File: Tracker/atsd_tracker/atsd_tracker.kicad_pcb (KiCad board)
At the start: 2 copper layers, 54 parts, among them J101 ICSP, J102 Battery, J103 SMA_PCB, Q101 IRLML2244, U101 MCP73821_2_SOT-23-5, U102 AZ1117CR-X.XTRG1, U103 DSPIC33CK64MC105, U104 AX5243, X101 16MHz, X102 8MHz

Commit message: Schematic done starting layout
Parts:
- added C121: 10pF, General_SMD:SM0402, F.Cu at (69.2, 87.8)
- added C122: 10pF, General_SMD:SM0402, F.Cu at (69.2, 90.5)
- added D103: RED, General_SMD:LED-0603, F.Cu at (92.2, 82.0)
- added D104: BLUE, General_SMD:LED-0603, F.Cu at (90.6, 82.0)
- added D105: GREEN, General_SMD:LED-0603, F.Cu at (89.0, 82.0)
- added J101: 5V Connector, Connector_JST:JST_XH_B2B-XH-A_1x02_P2.50mm_Vertical, F.Cu at (68.7, 109.4)
- added J103: Left side, Connector_PinHeader_1.27mm:PinHeader_2x05_P1.27mm_Vertical, F.Cu at (95.2, 83.6)
- added J104: Right side, Connector_PinHeader_1.27mm:PinHeader_2x05_P1.27mm_Vertical, F.Cu at (95.2, 105.6)
- added J106: SMA_PCB, Connectors_RF:SMA_RA_PCB_Amphenol, F.Cu at (61.6, 87.8)
- added L103: NC, General_SMD:SM0402, F.Cu at (120.6, 94.7)
- added L107: IND_0402, General_SMD:SM0402, F.Cu at (68.0, 88.2)
- added R103: 100, General_SMD:SM0402, F.Cu at (96.5, 86.5)
- added R104: 100, General_SMD:SM0402, F.Cu at (97.8, 86.5)
- added R105: 100, General_SMD:SM0402, F.Cu at (99.0, 86.5)
- added R106: 100, General_SMD:SM0402, F.Cu at (96.5, 108.4)
- added R107: 100, General_SMD:SM0402, F.Cu at (97.8, 108.4)
- added R108: 100, General_SMD:SM0402, F.Cu at (99.0, 108.4)
- added R110: 100, General_SMD:SM0402, F.Cu at (96.5, 79.5)
- added R111: 100, General_SMD:SM0402, F.Cu at (97.8, 79.5)
- added R112: 100, General_SMD:SM0402, F.Cu at (99.0, 79.5)
- added R113: 100, General_SMD:SM0402, F.Cu at (96.5, 101.7)
- added R114: 100, General_SMD:SM0402, F.Cu at (97.8, 101.7)
- added R115: 100, General_SMD:SM0402, F.Cu at (99.0, 101.7)
- added R118: 10, General_SMD:SM0402, F.Cu at (91.2, 111.8)
- added R119: NC, General_SMD:SM0402, F.Cu at (90.7, 110.3)
- added R120: 330, General_SMD:SM0402, F.Cu at (92.2, 84.6)
- added R121: 330, General_SMD:SM0402, F.Cu at (90.6, 84.6)
- added R122: 330, General_SMD:SM0402, F.Cu at (89.0, 84.6)
- added R125: 10R, General_SMD:SM0402, F.Cu at (70.5, 91.0)
- added R126: NC, General_SMD:SM0402, F.Cu at (72.7, 95.9)
- added R127: NC, General_SMD:SM0402, F.Cu at (71.6, 93.2)
- added R128: NC, General_SMD:SM0402, F.Cu at (71.6, 94.3)
- added TP101: TP1, Mounting_Holes:3.1mm_Plated, F.Cu at (134.0, 81.0)
- added TP102: TP1, Mounting_Holes:3.1mm_Plated, F.Cu at (61.0, 81.0)
- added TP103: TP1, Mounting_Holes:3.1mm_Plated, F.Cu at (134.0, 110.0)
- added TP104: TP1, Mounting_Holes:3.1mm_Plated, F.Cu at (61.0, 110.0)
- added U105: MAX-M8, UBlox:MAX-M8, F.Cu at (79.2, 91.0)
- C108: renamed from C106; footprint General_SMD:SM0603 -> General_SMD:SM0402
- C109: renamed from C107; footprint General_SMD:SM0603 -> General_SMD:SM0402
- C110: renamed from C108; footprint General_SMD:SM0603 -> General_SMD:SM0402
- C111: renamed from C109; footprint General_SMD:SM0603 -> General_SMD:SM0402
- C112: renamed from C110; footprint General_SMD:SM0603 -> General_SMD:SM0402
- R123: renamed from R106; footprint General_SMD:SM0603 -> General_SMD:SM0402
- R124: renamed from R107; footprint General_SMD:SM0603 -> General_SMD:SM0402
- U102: value AZ1117CR-X.XTRG1 -> XC6209F332MR-G; footprint SOT:SOT-89-3 -> SOT:SOT25-5
- moved C107 102.8 mm to (102.5, 102.5)
- moved X101 102.1 mm to (102.5, 100.2), turned to 180 degrees
- moved C106 100.7 mm to (105.0, 100.2), turned to -90 degrees
- moved U106 100.7 mm to (110.2, 94.0), turned to 180 degrees
- moved J102 96.2 mm to (84.4, 103.4), turned to 90 degrees
- moved C104 96.0 mm to (88.7, 111.2), turned to 90 degrees
- moved D102 94.6 mm to (84.4, 108.9), turned to -90 degrees
- moved C115 93.8 mm to (123.4, 94.3), turned to 90 degrees
- moved U102 92.6 mm to (90.2, 107.7)
- moved R116 92.0 mm to (93.4, 111.4), turned to -90 degrees
- moved R117 91.6 mm to (93.4, 108.9), turned to -90 degrees
- moved X102 91.1 mm to (110.8, 99.5), turned to 180 degrees
- moved C105 91.1 mm to (90.2, 104.7), turned to 180 degrees
- moved L101 91.0 mm to (124.9, 93.3), turned to 180 degrees
- moved C103 90.0 mm to (86.4, 107.9), turned to 90 degrees
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- renumbered C126 to C106, C127 to C107, C111 to C113, C112 to C114, C113 to C115, C114 to C116, C115 to C117, C116 to C118, C117 to C119, C118 to C120, C119 to C123, C120 to C124, C121 to C125, C122 to C126, C123 to C127, C124 to C128, C125 to C129, J103 to J105, J101 to J107, L103 to L104, L104 to L105, L105 to L106, L106 to L108, L107 to L109, L108 to L110, R103 to R109, R104 to R116, R105 to R117, U104 to U106, X102 to X101, X101 to X102
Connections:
- U102 pad 1: GND -> VCC
- U102 pad 2: VCC -> GND
- U102 pad 3: +3V3 -> Net-(R118-Pad2)
- U103 pad 1: unconnected-(U103-Pad1) -> /GPS_WAKE
- U103 pad 10: unconnected-(U103-Pad10) -> /left_4
- U103 pad 11: unconnected-(U103-Pad11) -> /left_5
- U103 pad 12: unconnected-(U103-Pad12) -> /BMON
- U103 pad 15: unconnected-(U103-Pad15) -> /RF_IRQ
- U103 pad 16: unconnected-(U103-Pad16) -> /right_0
- U103 pad 17: unconnected-(U103-Pad17) -> /right_1
- U103 pad 2: unconnected-(U103-Pad2) -> /GPS_PPS
- U103 pad 20: unconnected-(U103-Pad20) -> /right_2
- U103 pad 23: unconnected-(U103-Pad23) -> /right_3
- U103 pad 24: unconnected-(U103-Pad24) -> /right_4
- U103 pad 25: unconnected-(U103-Pad25) -> /right_5
- U103 pad 26: /RF_IRQ -> unconnected-(U103-Pad26)
- U103 pad 3: unconnected-(U103-Pad3) -> /GPS_RXD
- U103 pad 36: unconnected-(U103-Pad36) -> /GPS_SCL
- U103 pad 37: unconnected-(U103-Pad37) -> /GPS_SDA
- U103 pad 4: unconnected-(U103-Pad4) -> /GPS_TXD
- U103 pad 46: unconnected-(U103-Pad46) -> Net-(R120-Pad1)
- U103 pad 47: unconnected-(U103-Pad47) -> Net-(R121-Pad1)
- U103 pad 48: unconnected-(U103-Pad48) -> Net-(R122-Pad1)
- U103 pad 6: unconnected-(U103-Pad6) -> /left_0
- U103 pad 7: unconnected-(U103-Pad7) -> /left_1
- U103 pad 8: unconnected-(U103-Pad8) -> /left_2
- U103 pad 9: unconnected-(U103-Pad9) -> /left_3
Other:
- board outline added: 81 x 37 mm
- copper layers 2 -> 4
- board text added: "+"
- board text added: "-"
- board text added: "BAT"

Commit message: Produced prototype
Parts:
- moved C111 0.85 mm to (102.5, 92.9), turned to -90 degrees
- moved C125 0.40 mm to (110.5, 89.7)
- moved L110 0.40 mm to (110.5, 90.4)
- renumbered C123 to locked
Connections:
- net Net-(C116-Pad1) renamed /R2_N
- net Net-(C117-Pad2) renamed /R2_P
- net Net-(C119-Pad1) renamed /R0_P
- net Net-(C119-Pad2) renamed /R1_P
- net Net-(C120-Pad1) renamed /R0_N
- net Net-(C120-Pad2) renamed /R1_N
- U103 pad 10: /left_4 -> unconnected-(U103-Pad10)
- U103 pad 11: /left_5 -> unconnected-(U103-Pad11)
- U103 pad 38: unconnected-(U103-Pad38) -> /left_5
- U103 pad 39: unconnected-(U103-Pad39) -> /left_4
- U103 pad 40: unconnected-(U103-Pad40) -> /left_3
- U103 pad 45: unconnected-(U103-Pad45) -> Net-(R120-Pad1)
- U103 pad 46: Net-(R120-Pad1) -> Net-(R121-Pad1)
- U103 pad 47: Net-(R121-Pad1) -> Net-(R122-Pad1)
- U103 pad 48: Net-(R122-Pad1) -> /GPS_~{RST}
- U103 pad 9: /left_3 -> unconnected-(U103-Pad9)
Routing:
- net VCC: track 0.00 -> 92.4 mm, vias 0 -> 3
- net /PGD: track 0.00 -> 41.6 mm, vias 0 -> 1
- net /GPS_SCL: track 0.00 -> 38.3 mm, vias 0 -> 2
- net /PGC: track 0.00 -> 36.8 mm, vias 0 -> 1
- net /GPS_SDA: track 0.00 -> 35.3 mm, vias 0 -> 2
- net +5V: track 0.00 -> 30.1 mm
- net +3V3: track 0.00 -> 29.2 mm, vias 0 -> 16
- net /left_2: track 0.00 -> 28.4 mm, vias 0 -> 2
- net /left_1: track 0.00 -> 25.9 mm, vias 0 -> 2
- net /~{MCLR}: track 0.00 -> 25.4 mm, vias 0 -> 1
- net /right_5: track 0.00 -> 24.4 mm, vias 0 -> 2
- net /left_0: track 0.00 -> 22.5 mm, vias 0 -> 2
- net /right_4: track 0.00 -> 22.5 mm, vias 0 -> 2
- net /right_3: track 0.00 -> 21.9 mm, vias 0 -> 2
- net /BMON: track 0.00 -> 17.3 mm
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- added copper zone on F.Cu, net +3V3
- added copper zone on In2.Cu, net +3V3
- added copper zone on B.Cu, net GND
- added copper zone on F.Cu, net GND
- added copper zone on In1.Cu, net GND
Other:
- board text added: "ATDS V0.1 APRS Compliant System F4IHX - CC-BY-SA"

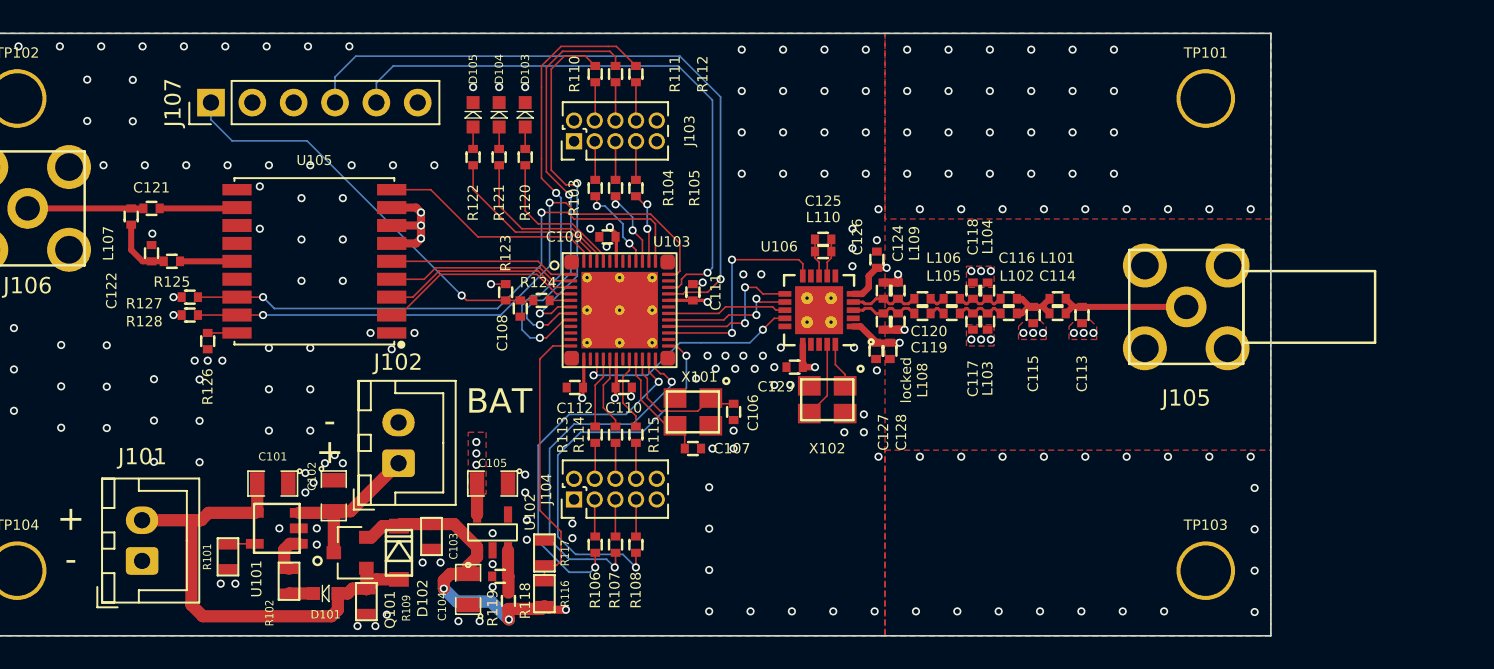
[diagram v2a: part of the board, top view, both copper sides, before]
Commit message: OnSemi discontinued AX5043 and all sub-ghz, switching to si446x
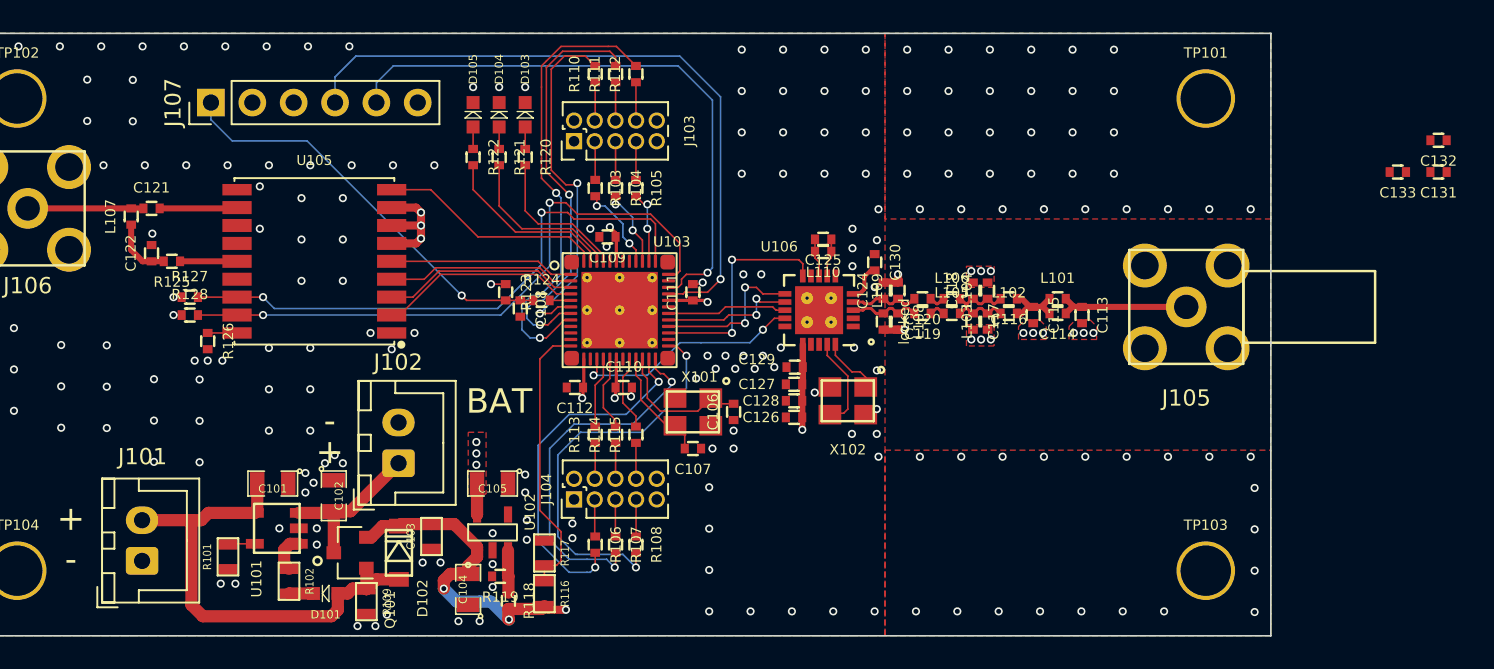
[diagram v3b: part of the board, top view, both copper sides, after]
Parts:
- added C130: 100pF, General_SMD:SM0402, F.Cu at (113.7, 91.1)
- added C131: 100pF, General_SMD:SM0402, F.Cu at (148.3, 85.5)
- added C132: 10pF, General_SMD:SM0402, F.Cu at (148.3, 83.6)
- added C133: 10pF, General_SMD:SM0402, F.Cu at (145.8, 85.5)
- moved C126 10.9 mm to (108.7, 100.6), turned to 0 degrees
- moved C128 6.64 mm to (108.7, 99.6), turned to 0 degrees
- moved C127 5.44 mm to (108.7, 98.6), turned to 0 degrees
- moved X102 1.27 mm to (112.0, 99.6)
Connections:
- U106 pad 1: +3V3 -> Net-(U106-Pad1)
- U106 pad 5: +3V3 -> Net-(U106-Pad5)
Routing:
- net +3V3: track 29.2 -> 25.9 mm, vias 16 -> 14
- net Net-(U106-Pad5): track 0.00 -> 2.36 mm
- net Net-(U106-Pad19): track 4.71 -> 5.74 mm
- net Net-(U106-Pad20): track 2.80 -> 3.69 mm
